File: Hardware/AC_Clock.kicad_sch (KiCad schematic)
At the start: 33 parts, among them T1 10:1, U1 AZ1117-5.0, U2 LTV-817S, U3 4040, U4 74LS393, U5 74LS393

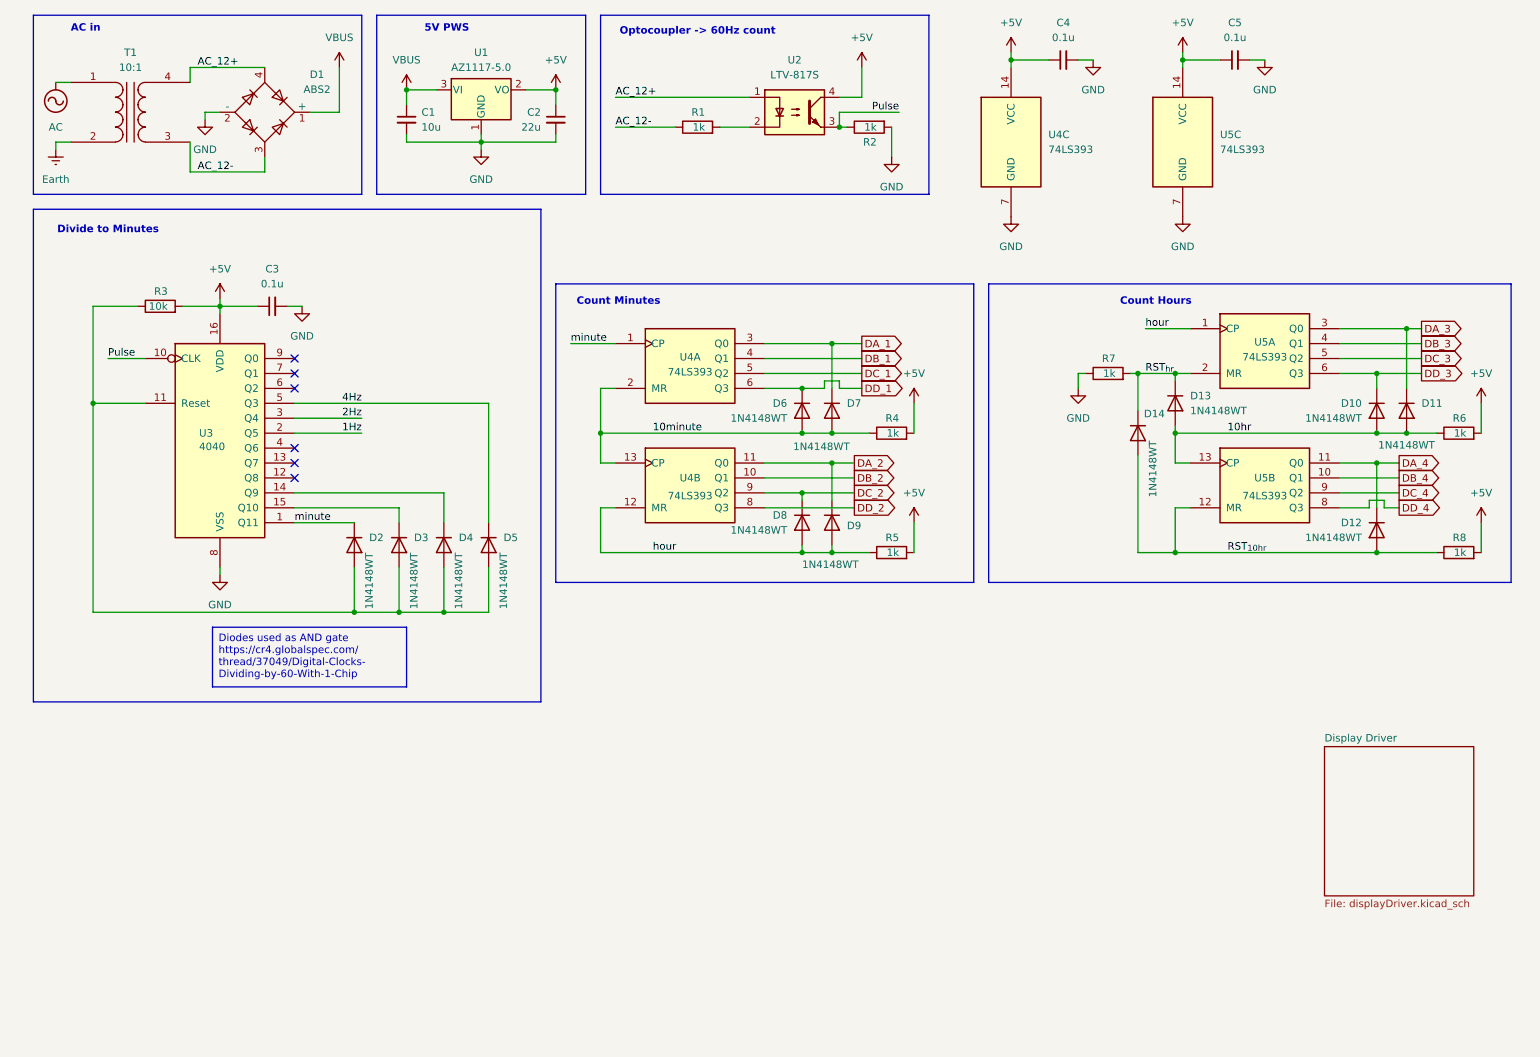
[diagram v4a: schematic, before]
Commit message: Add pushbuttons to be able to set time
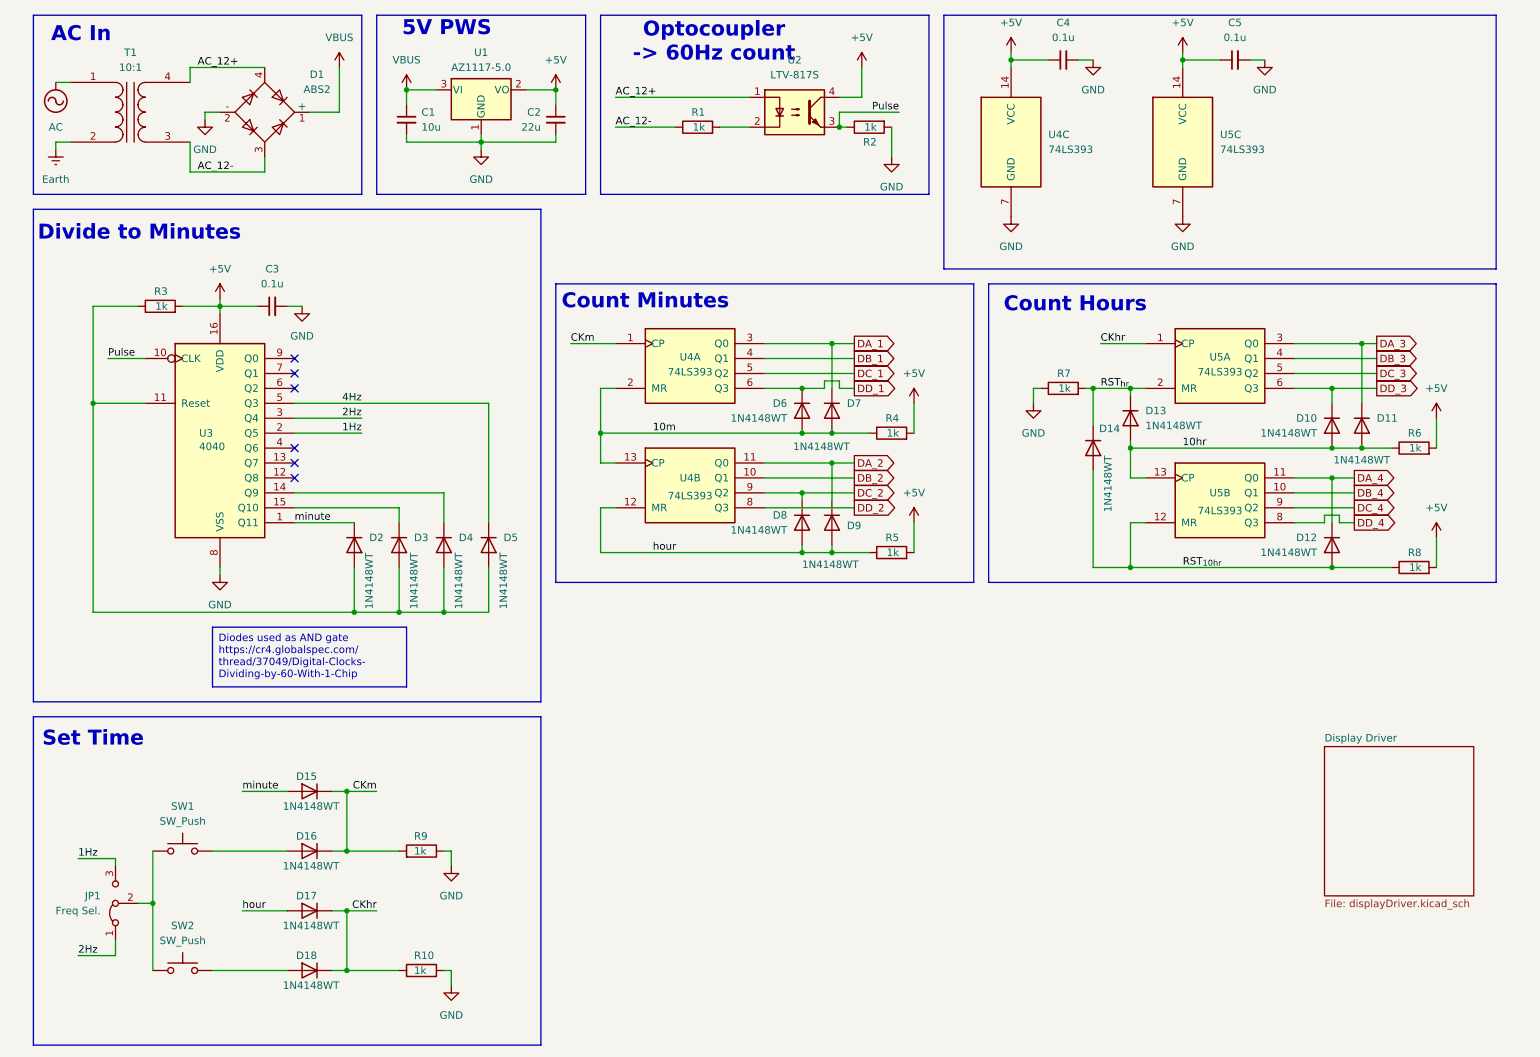
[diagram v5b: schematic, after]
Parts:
- added D15, D16, D17, D18: 1N4148WT, Diode_SMD:D_SOD-523, symbol Diode:1N4148WT
- added JP1: Freq Sel., symbol Jumper:Jumper_3_Bridged12
- added R10, R9: 1k, symbol Device:R
- added SW1, SW2: SW_Push, symbol Switch:SW_Push
- R3: value 10k -> 1k
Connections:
- net 1Hz: now also JP1.3 (B)
- net 2Hz: now also JP1.1 (A)
- net GND: now also R10.1, R9.1
- net hour: now also D17.2 (A); no longer U5.1 (CP)
- net minute: now also D15.2 (A); no longer U4.1 (CP)
- net 10minute renamed 10m
- new net: JP1.2 (C), SW1.1, SW2.1
- new net: D16.2 (A), SW1.2
- new net: D18.2 (A), SW2.2
- new net CKhr: D17.1 (K), D18.1 (K), R10.2, U5.1 (CP)
- new net CKm: D15.1 (K), D16.1 (K), R9.2, U4.1 (CP)
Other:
- note added: "AC In"
- note added: "Set Time"
- note removed: "AC in"
- moved on the sheet: D10, D11, D12, D13, D14, R6, R7, R8, U5A, U5B

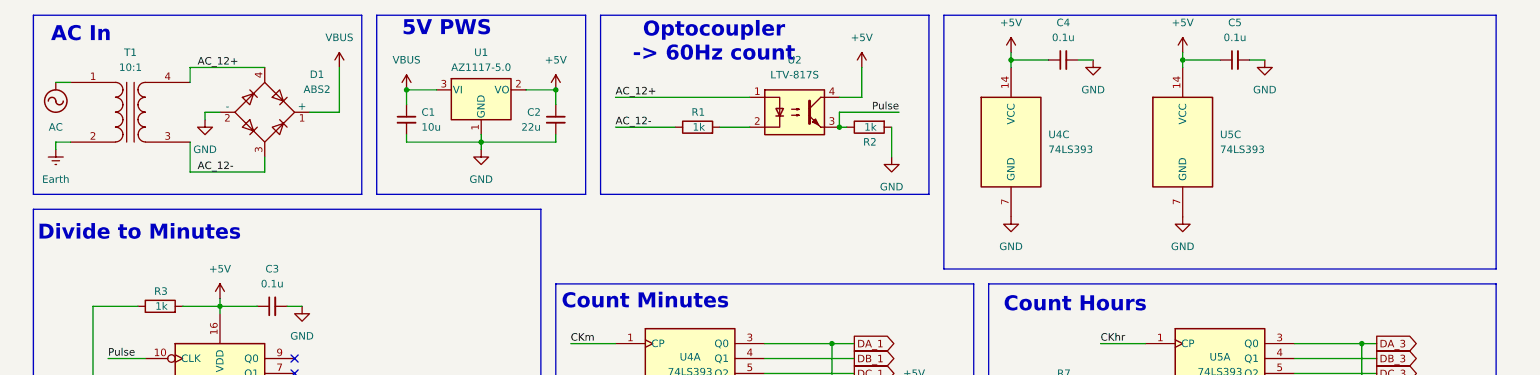
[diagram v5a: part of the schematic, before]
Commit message: Set Footprints for components
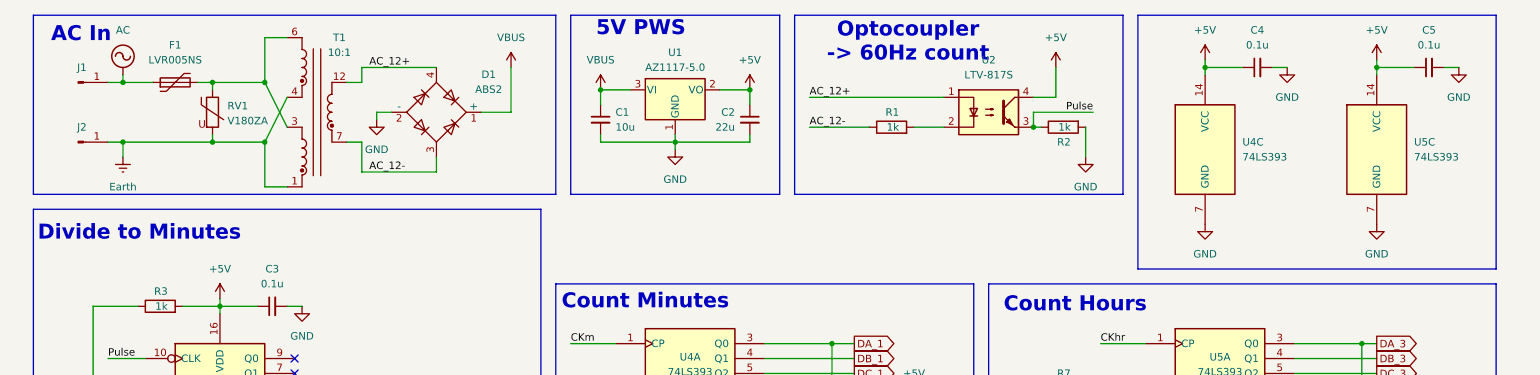
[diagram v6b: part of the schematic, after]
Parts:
- added F1: LVR005NS, Fuse:Fuse_BelFuse_0ZRE0005FF_L8.3mm_W3.8mm, symbol Device:Polyfuse
- added J1: L, JKC_Library:Keystone_1287, symbol Connector:Conn_01x01_Pin
- added J2: N, JKC_Library:Keystone_1287, symbol Connector:Conn_01x01_Pin
- added RV1: V180ZA, Varistor:RV_Disc_D7mm_W5.1mm_P5mm, symbol Device:Varistor
- C1, C2, C3, C4, C5: footprint (none) -> Capacitor_SMD:C_0603_1608Metric
- JP1: footprint (none) -> Jumper:SolderJumper-3_P1.3mm_Bridged12_RoundedPad1.0x1.5mm
- R1, R10, R2, R3, R4, R5, R6, R7, R8, R9: footprint (none) -> Resistor_SMD:R_0805_2012Metric
- SW1, SW2: footprint (none) -> Button_Switch_SMD:SW_SPST_PTS645
- T1: footprint (none) -> JKC_Library:Transformer_CL2-5.0R-12; symbol Device:Transformer_1P_1S -> JKC_library:CL2-x
- U3: footprint (none) -> Package_DIP:DIP-16_W7.62mm
- U4, U5: footprint (none) -> Package_DIP:DIP-14_W7.62mm
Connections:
- net AC: now also F1.1, J1.1 (Pin_1); no longer T1.1 (AA)
- net AC_12+: now also T1.12; no longer T1.4 (SB)
- net AC_12-: now also T1.7; no longer T1.3 (SA)
- net Earth: now also T1.1, T1.4, J2.1 (Pin_1), RV1.2; no longer T1.2 (AB)
- new net: F1.2, RV1.1, T1.3, T1.6
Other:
- moved on the sheet: C1, C2, C4, C5, D1, R1, R2, U1, U2, U4C, U5C

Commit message: Work on routing
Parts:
- removed D12: 1N4148WT, Diode_SMD:D_SOD-523, symbol Diode:1N4148WT
- removed R8: 1k, Resistor_SMD:R_0805_2012Metric, symbol Device:R
- R1, R10, R2, R3, R4, R5, R6, R7, R9: footprint Resistor_SMD:R_0805_2012Metric -> Resistor_SMD:R_0603_1608Metric
- SW1: value SW_Push -> Min_PB
- SW2: value SW_Push -> Hr_PB
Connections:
- net RST_{10hr} is gone; now on net DA_4: D14.2 (A), U5.12 (MR)
- net minute: now also D2.2 (A), D3.2 (A), D4.2 (A), D5.2 (A), R3.1, U3.11 (Reset); no longer D2.1 (K), U3.1 (Q11)
- net SetM: now reaches D16.2 (A), SW1.2
- net SetH: now reaches D18.2 (A), SW2.2
- net 8s: now reaches D4.1 (K), U3.14 (Q9)
- net 16s: now reaches D3.1 (K), U3.15 (Q10)
- net Fused: now reaches F1.2, RV1.1, T1.3, T1.6
- new net 32s: D2.1 (K), U3.1 (Q11)

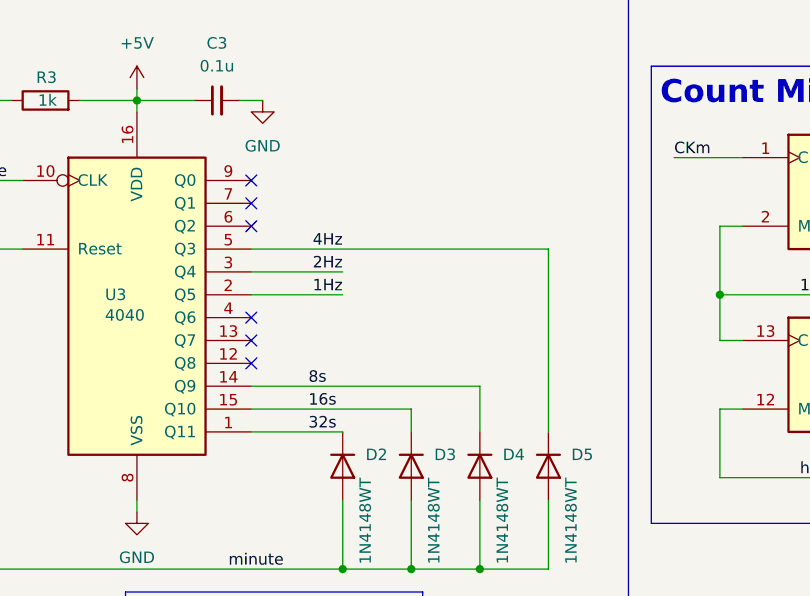
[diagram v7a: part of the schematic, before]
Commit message: Add in correct calculated times for frequency divider
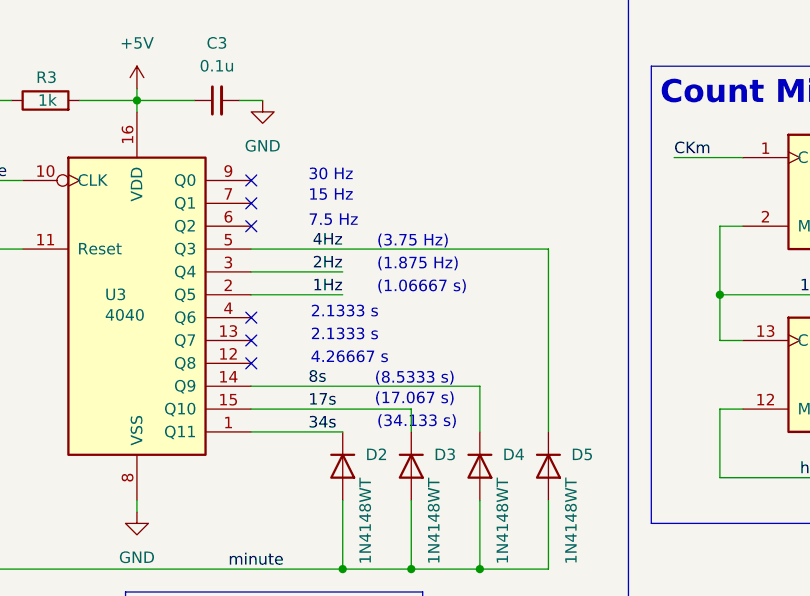
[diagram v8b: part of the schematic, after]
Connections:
- net 16s renamed 17s
- net 32s renamed 34s
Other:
- note added: "(1.06667 s)"
- note added: "(1.875 Hz)"
- note added: "(17.067 s)"
- note added: "(3.75 Hz)"
- note added: "(34.133 s)"
- note added: "(8.5333 s)"
- note added: "15 Hz"
- note added: "2.1333 s"
- note added: "30 Hz"
- note added: "4.26667 s"
- note added: "7.5 Hz"
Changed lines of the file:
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@@
+		)
+	)
+	(text "30 Hz"
+		(exclude_from_sim no)
+		(at 66.04 73.914 0)
+		(effects
+			(font
+				(size 1.27 1.27)
+			)
+			(justify left bottom)
+		)
+	)
+	(text "(34.133 s)"
+		(exclude_from_sim no)
+		(at 73.66 101.346 0)
+		(effects
+			(font
+				(size 1.27 1.27)
+			)
+			(justify left bottom)
+		)
+	)
+	(text "(17.067 s)"
+		(exclude_from_sim no)
+		(at 73.406 98.806 0)
+		(effects
+			(font
+				(size 1.27 1.27)
+			)
+			(justify left bottom)
+		)
+	)
+	(text "(1.875 Hz)"
+		(exclude_from_sim no)
+		(at 73.66 83.82 0)
+		(effects
+			(font
+				(size 1.27 1.27)
+			)
+			(justify left bottom)
 		)
 	)
@@
 		)
 	)
+	(text "(3.75 Hz)"
+		(exclude_from_sim no)
+		(at 73.66 81.28 0)
+		(effects
+			(font
+				(size 1.27 1.27)
+			)
+			(justify left bottom)
+		)
+	)
+	(text "15 Hz"
+		(exclude_from_sim no)
+		(at 66.04 76.2 0)
+		(effects
+			(font
+				(size 1.27 1.27)
+			)
+			(justify left bottom)
+		)
+	)
 	(text "Optocoupler \n-> 60Hz count"
 		(exclude_from_sim no)
@@
 		)
 	)
+	(text "(8.5333 s)"
+		(exclude_from_sim no)
+		(at 73.406 96.52 0)
+		(effects
+			(font
+				(size 1.27 1.27)
+			)
+			(justify left bottom)
+		)
+	)
 	(text "Set Time"
 		(exclude_from_sim no)
@@
 		)
 	)
+	(text "2.1333 s"
+		(exclude_from_sim no)
+		(at 66.294 89.154 0)
+		(effects
+			(font
+				(size 1.27 1.27)
+			)
+			(justify left bottom)
+		)
+	)
+	(text "7.5 Hz"
+		(exclude_from_sim no)
+		(at 66.04 78.994 0)
+		(effects
+			(font
+				(size 1.27 1.27)
+			)
+			(justify left bottom)
+		)
+	)
+	(text "4.26667 s"
+		(exclude_from_sim no)
+		(at 66.294 94.234 0)
+		(effects
+			(font
+				(size 1.27 1.27)
+			)
+			(justify left bottom)
+		)
+	)
 	(text "Divide to Minutes"
 		(exclude_from_sim no)
@@
 		)
 	)
+	(text "(1.06667 s)"
+		(exclude_from_sim no)
+		(at 73.66 86.36 0)
+		(effects
+			(font
+				(size 1.27 1.27)
+			)
+			(justify left bottom)
+		)
+	)
 	(text "AC In"
 		(exclude_from_sim no)
@@
 				(bold yes)
 			)
+		)
+	)
+	(text "2.1333 s"
+		(exclude_from_sim no)
+		(at 66.294 91.694 0)
+		(effects
+			(font
+				(size 1.27 1.27)
+			)
+			(justify left bottom)
 		)
 	)
@@
 		)
 	)
-	(label "16s"
+	(label "17s"
 		(at 66.04 99.06 0)
 		(fields_autoplaced yes)
@@
 		)
 	)
-	(label "32s"
+	(label "34s"
 		(at 66.04 101.6 0)
 		(fields_autoplaced yes)
